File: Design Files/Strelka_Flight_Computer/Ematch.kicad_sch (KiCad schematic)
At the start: 16 parts

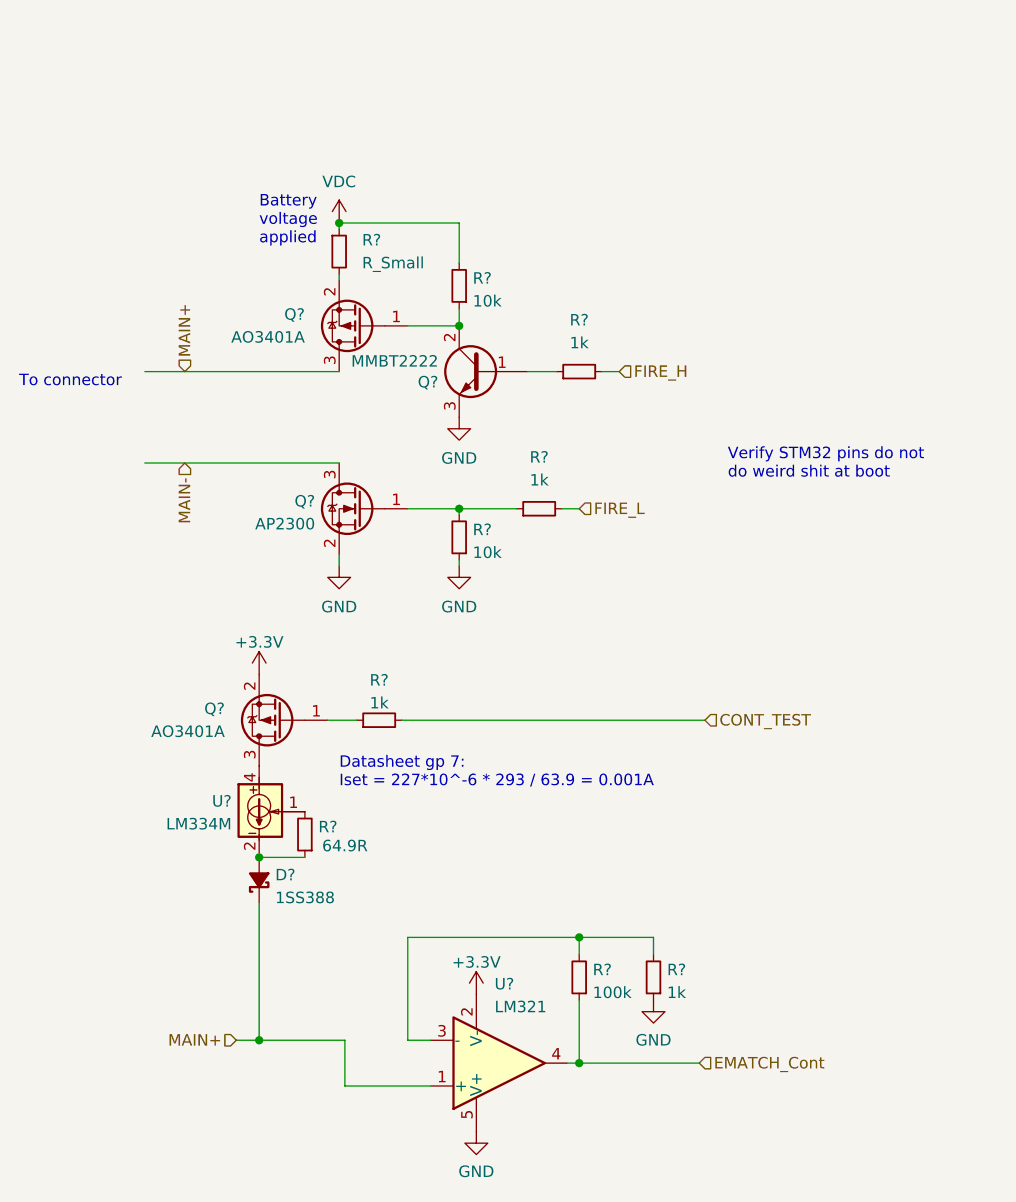
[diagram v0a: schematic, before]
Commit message: Added motor driver to power board
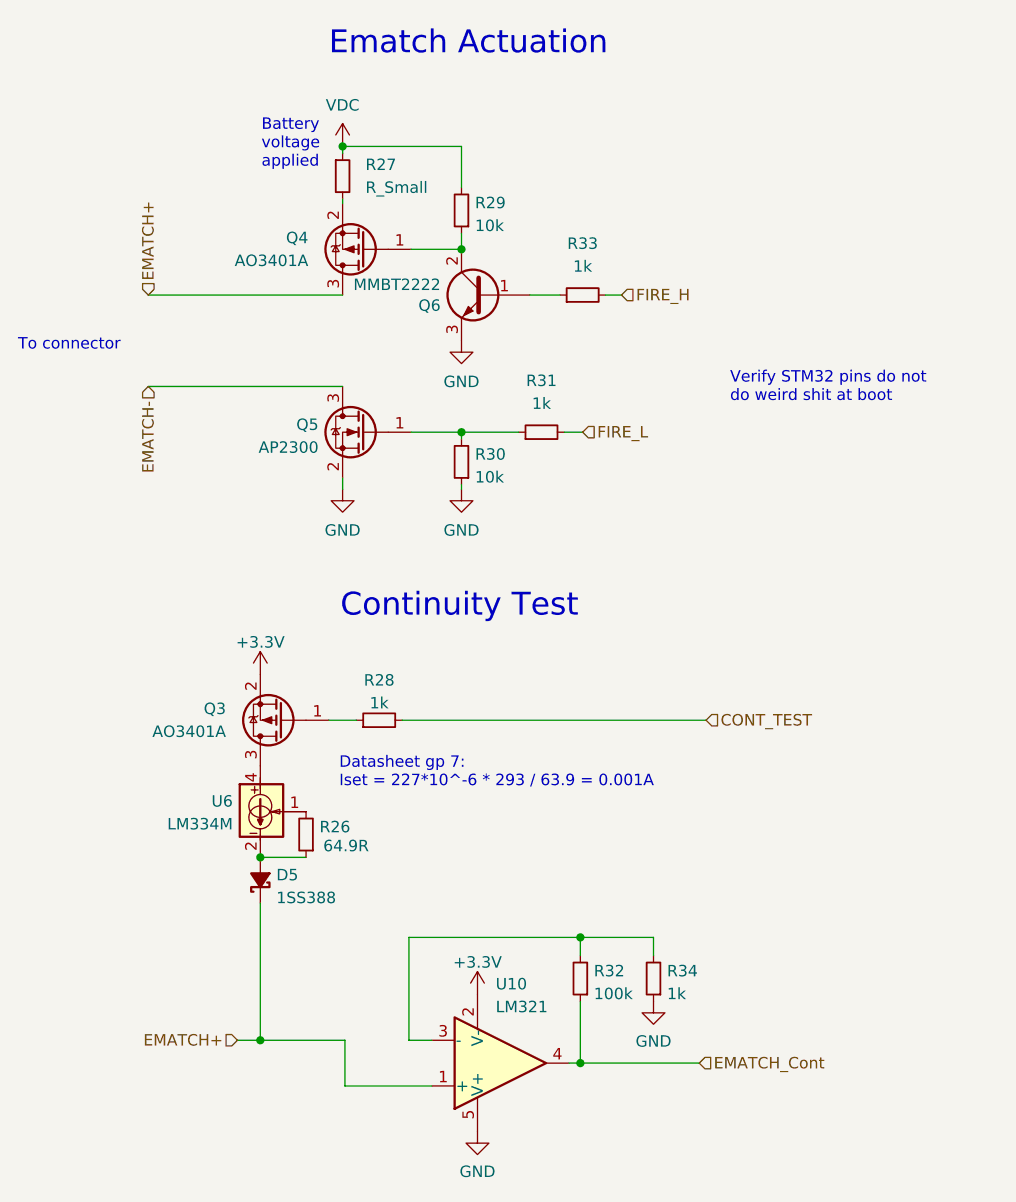
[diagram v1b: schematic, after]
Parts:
- gave numbers to parts that had none: 16
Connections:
- net MAIN+ renamed EMATCH+
- net MAIN- renamed EMATCH-
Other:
- note added: "Continuity Test"
- note added: "Ematch Actuation"
- moved on the sheet: Q4, Q5, Q6, R27, R29, R30, R31, R33

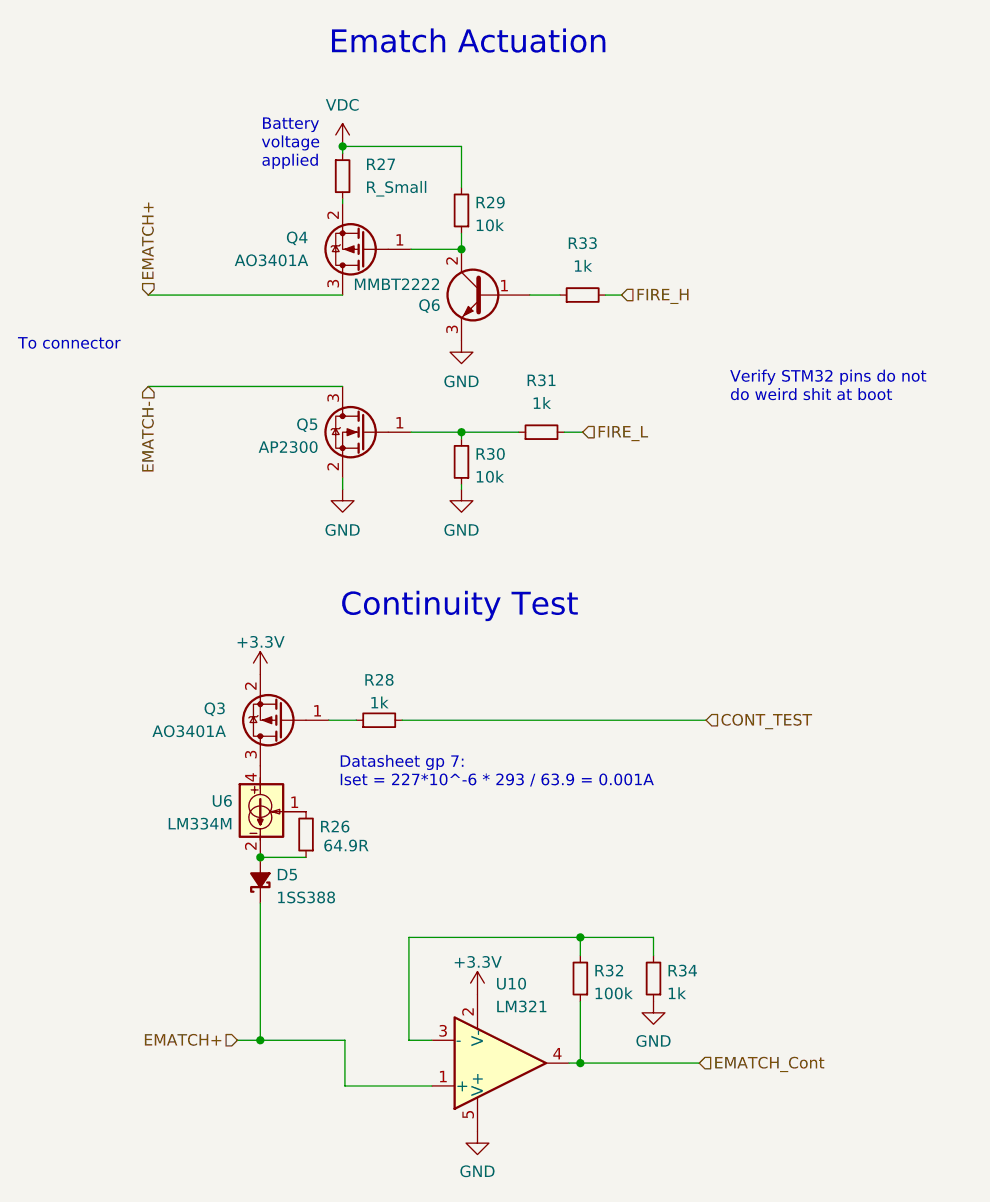
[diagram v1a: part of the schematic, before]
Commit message: Switched order of pull-down resistor into ematch mostfet sw
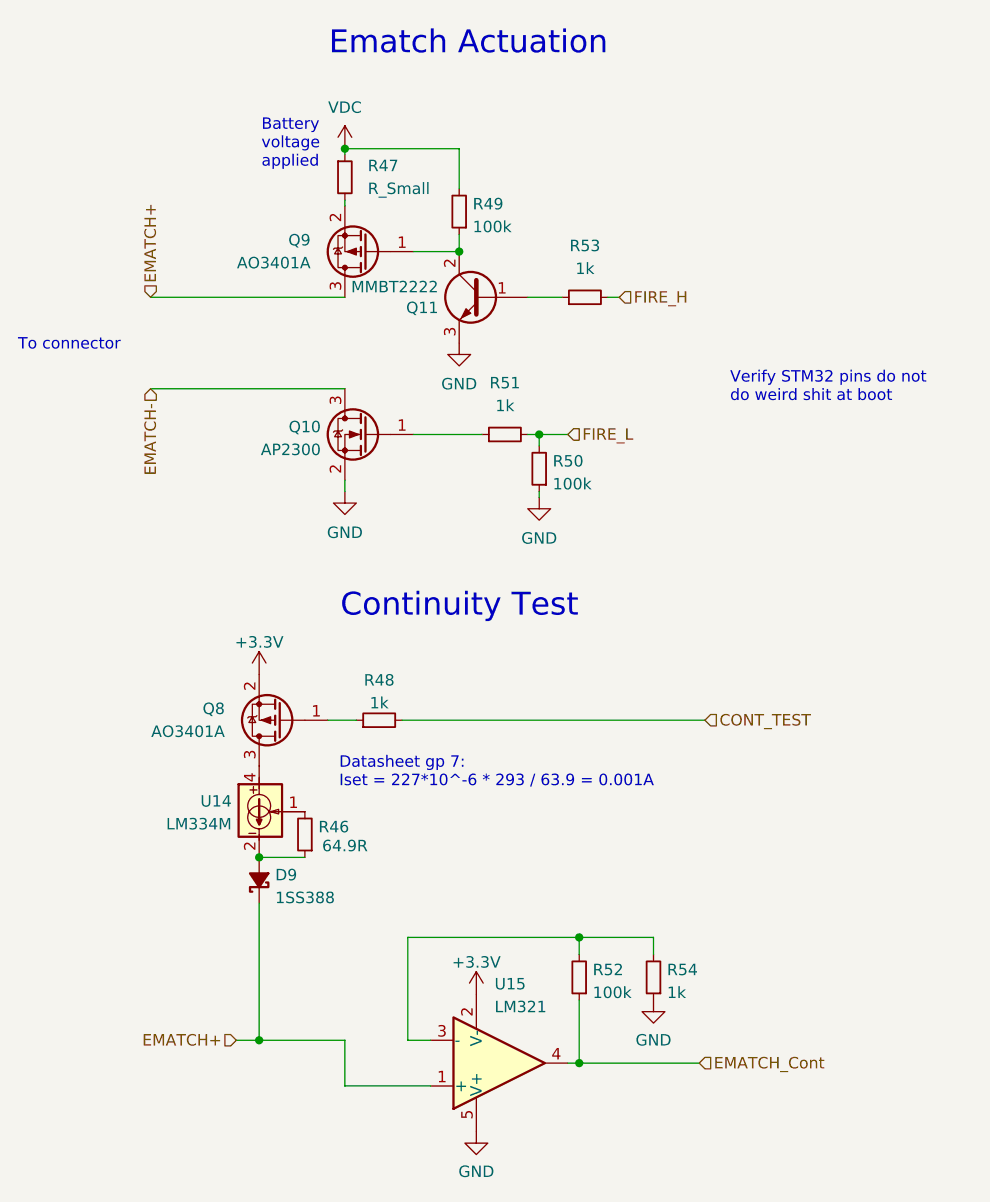
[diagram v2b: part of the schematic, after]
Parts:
- R49: renamed from R29; value 10k -> 100k
- R50: renamed from R30; value 10k -> 100k
- renumbered D5 to D9, Q5 to Q10, Q6 to Q11, Q3 to Q8, Q4 to Q9, R26 to R46, R27 to R47, R28 to R48, R31 to R51, R32 to R52, R33 to R53, R34 to R54, U6 to U14, U10 to U15
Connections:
- net FIRE_L: now also R50.2
- net at Q10.1 (G), R51.1: no longer R50.2
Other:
- moved on the sheet: R50, R51

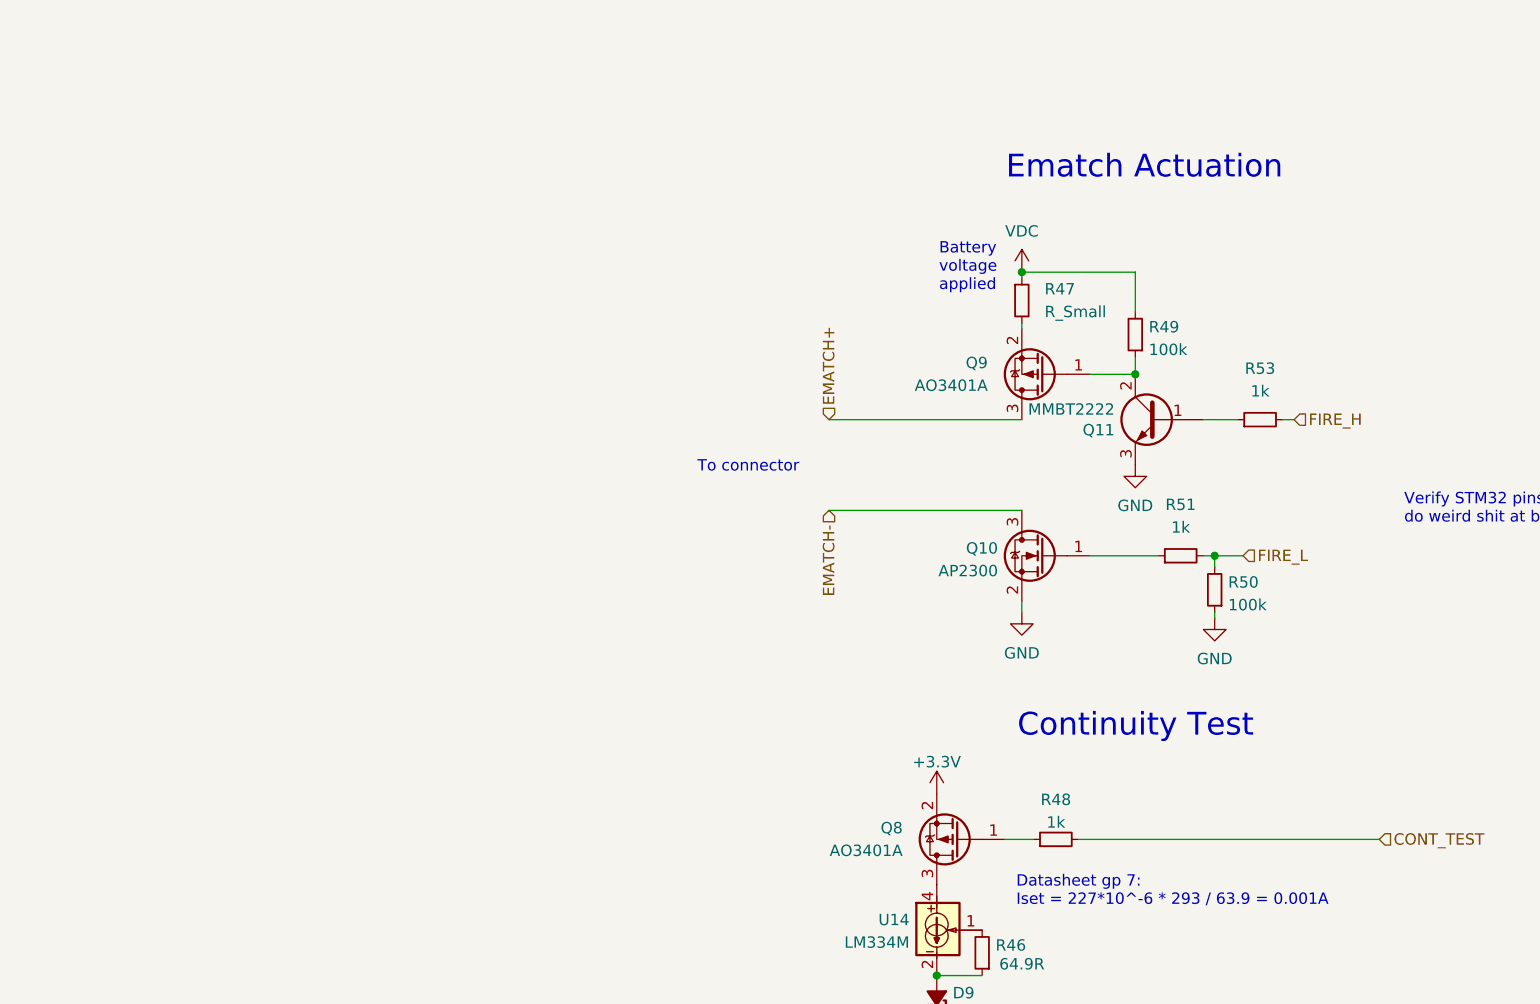
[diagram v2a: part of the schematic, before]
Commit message: Changed boost converter
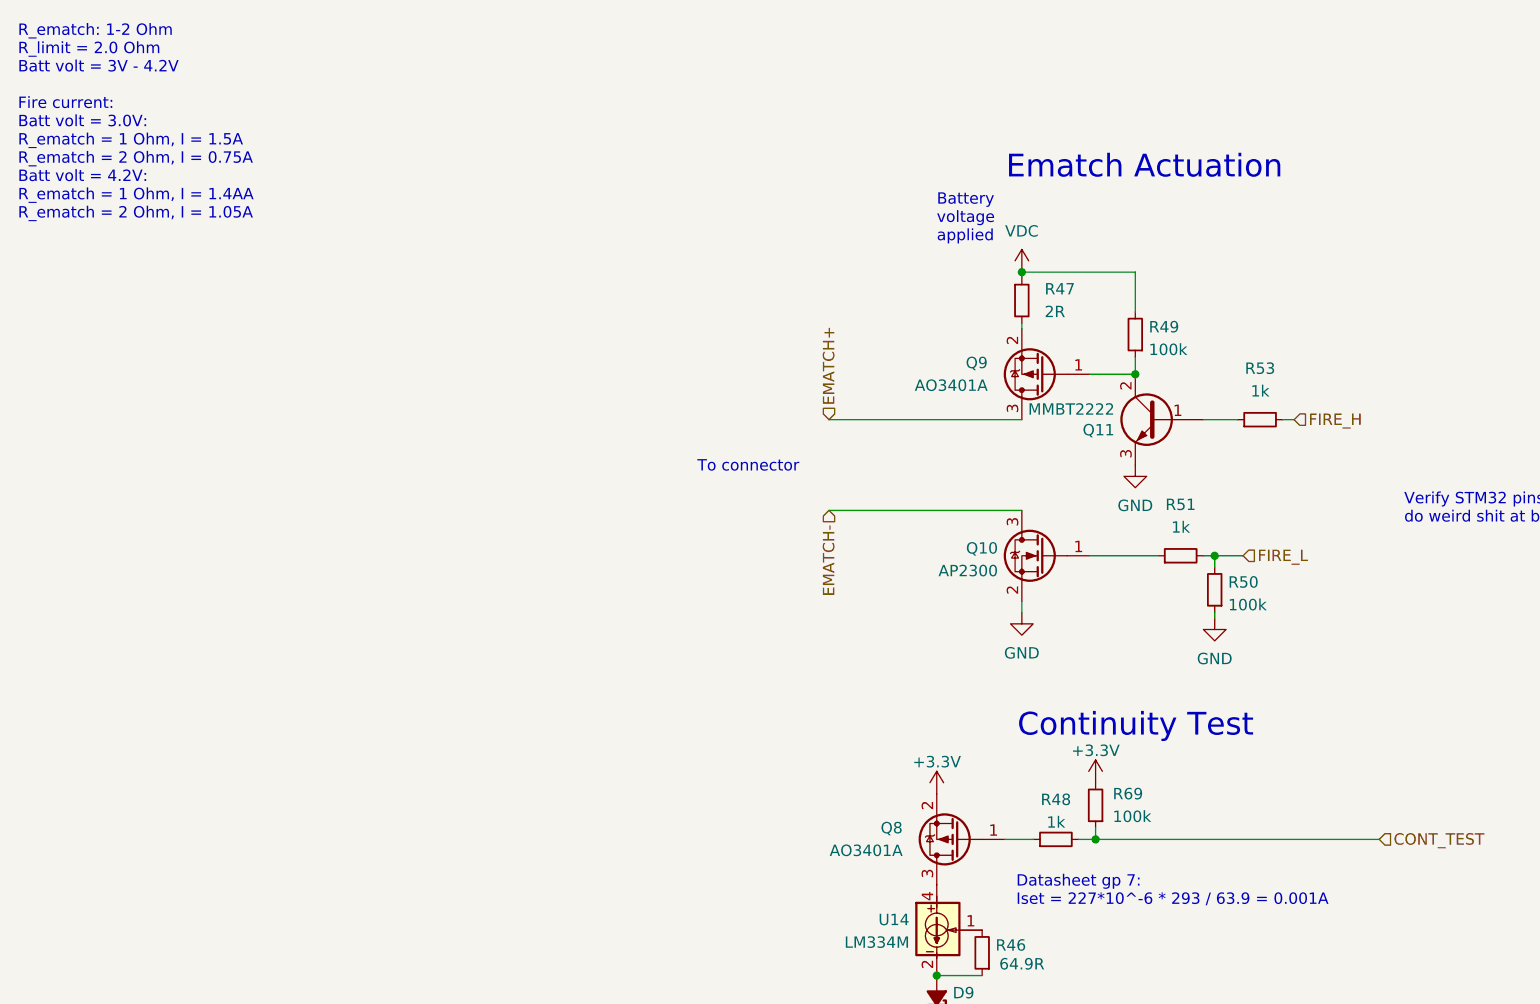
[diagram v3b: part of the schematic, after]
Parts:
- added R69: 100k, Resistor_SMD:R_0603_1608Metric, symbol Device:R_Small
- R47: value R_Small -> 2R; footprint (none) -> Resistor_SMD:R_2512_6332Metric; LCSC# (none) -> C91926
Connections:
- net +3V3: now also R69.2
- net CONT_TEST: now also R69.1
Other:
- note added: "R_ematch: 1-2 Ohm R_limit = 2.0 Ohm Batt volt = 3V - 4.2V Fire current: Batt volt = 3.0V: R_ematch = 1 Ohm, I = 1.5A R_ematch = 2 Ohm, I = 0.75A Batt volt = 4.2V: R_ematch = 1 Ohm, I = 1.4AA R_ematch = 2 Ohm, I = 1.05A"
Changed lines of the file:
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@@
   (junction (at 117.475 142.24) (diameter 0) (color 0 0 0 0)
   )
+  (junction (at 135.255 106.68) (diameter 0) (color 0 0 0 0)
+  )
   (junction (at 139.7 54.61) (diameter 0) (color 0 0 0 0)
   )
@@
     (stroke (width 0) (type default) (color 0 0 0 0))
   )
+  (wire (pts (xy 135.255 105.41) (xy 135.255 106.68))
+    (stroke (width 0) (type default) (color 0 0 0 0))
+  )
   (wire (pts (xy 153.035 130.81) (xy 161.29 130.81))
     (stroke (width 0) (type default) (color 0 0 0 0))
@@
     (stroke (width 0) (type default) (color 0 0 0 0))
   )
-  (wire (pts (xy 133.35 106.68) (xy 167.005 106.68))
+  (wire (pts (xy 133.35 106.68) (xy 135.255 106.68))
     (stroke (width 0) (type default) (color 0 0 0 0))
   )
@@
   )
   (wire (pts (xy 148.59 74.93) (xy 148.59 76.2))
+    (stroke (width 0) (type default) (color 0 0 0 0))
+  )
+  (wire (pts (xy 135.255 106.68) (xy 167.005 106.68))
     (stroke (width 0) (type default) (color 0 0 0 0))
   )
@@
     (effects (font (size 1.27 1.27)) (justify left bottom))
   )
-  (text "Battery \nvoltage \napplied" (at 117.729 45.466 0)
+  (text "Battery \nvoltage \napplied" (at 117.475 40.005 0)
+    (effects (font (size 1.27 1.27)) (justify left bottom))
+  )
+  (text "R_ematch: 1-2 Ohm\nR_limit = 2.0 Ohm\nBatt volt = 3V - 4.2V\n\nFire current:\nBatt volt = 3.0V: \nR_ematch = 1 Ohm, I = 1.5A\nR_ematch = 2 Ohm, I = 0.75A\nBatt volt = 4.2V:\nR_ematch = 1 Ohm, I = 1.4AA\nR_ematch = 2 Ohm, I = 1.05A\n"
+    (at 14.605 37.465 0)
     (effects (font (size 1.27 1.27)) (justify left bottom))
   )
@@
     )
     (pin "1")
+  )
+  (symbol (lib_id "Device:R_Small") (at 135.255 102.87 180)
+    (in_bom yes) (on_board yes) (fields_autoplaced)
+    (property "Reference" "R69" (id 0) (at 137.16 101.5999 0)
+      (effects (font (size 1.27 1.27)) (justify right))
+    )
+    (property "Value" "100k" (id 1) (at 137.16 104.1399 0)
+      (effects (font (size 1.27 1.27)) (justify right))
+    )
+    (property "Footprint" "Resistor_SMD:R_0603_1608Metric" (id 2) (at 135.255 102.87 0)
+      (effects (font (size 1.27 1.27)) hide)
+    )
+    (property "Datasheet" "~" (id 3) (at 135.255 102.87 0)
+      (effects (font (size 1.27 1.27)) hide)
+    )
+    (pin "1")
+    (pin "2")
   )
   (symbol (lib_id "power:GND") (at 161.29 137.795 0)
@@
     (pin "3")
   )
+  (symbol (lib_id "power:+3.3V") (at 135.255 100.33 0)
+    (in_bom yes) (on_board yes) (fields_autoplaced)
+    (property "Reference" "#PWR0226" (id 0) (at 135.255 104.14 0)
+      (effects (font (size 1.27 1.27)) hide)
+    )
+    (property "Value" "+3.3V" (id 1) (at 135.255 96.7542 0))
+    (property "Footprint" "" (id 2) (at 135.255 100.33 0)
+      (effects (font (size 1.27 1.27)) hide)
+    )
+    (property "Datasheet" "" (id 3) (at 135.255 100.33 0)
+      (effects (font (size 1.27 1.27)) hide)
+    )
+    (pin "1")
+  )
   (symbol (lib_id "power:+3.3V") (at 117.475 101.6 0)
     (in_bom yes) (on_board yes) (fields_autoplaced)
@@
       (effects (font (size 1.27 1.27)) (justify left))
     )
-    (property "Value" "R_Small" (id 1) (at 129.54 47.6249 0)
-      (effects (font (size 1.27 1.27)) (justify left))
-    )
-    (property "Footprint" "" (id 2) (at 127 46.355 0)
-      (effects (font (size 1.27 1.27)) hide)
-    )
-    (property "Datasheet" "~" (id 3) (at 127 46.355 0)
-      (effects (font (size 1.27 1.27)) hide)
-    )
+    (property "Value" "2R" (id 1) (at 129.54 47.6249 0)
+      (effects (font (size 1.27 1.27)) (justify left))
+    )
+    (property "Footprint" "Resistor_SMD:R_2512_6332Metric" (id 2) (at 127 46.355 0)
+      (effects (font (size 1.27 1.27)) hide)
+    )
+    (property "Datasheet" "https://lcsc.com/product-detail/Chip-span-style-background-color-ff0-Resistor-span-Surface-Mount_UNI-ROYAL-Uniroyal-Elec-HP122WF200KT4E_C91926.html" (id 3) (at 127 46.355 0)
+      (effects (font (size 1.27 1.27)) hide)
+    )
+    (property "LCSC#" "C91926" (id 4) (at 127 46.355 0)
+      (effects (font (size 1.27 1.27)) hide)
+    )
